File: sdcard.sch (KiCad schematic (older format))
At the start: 4 parts

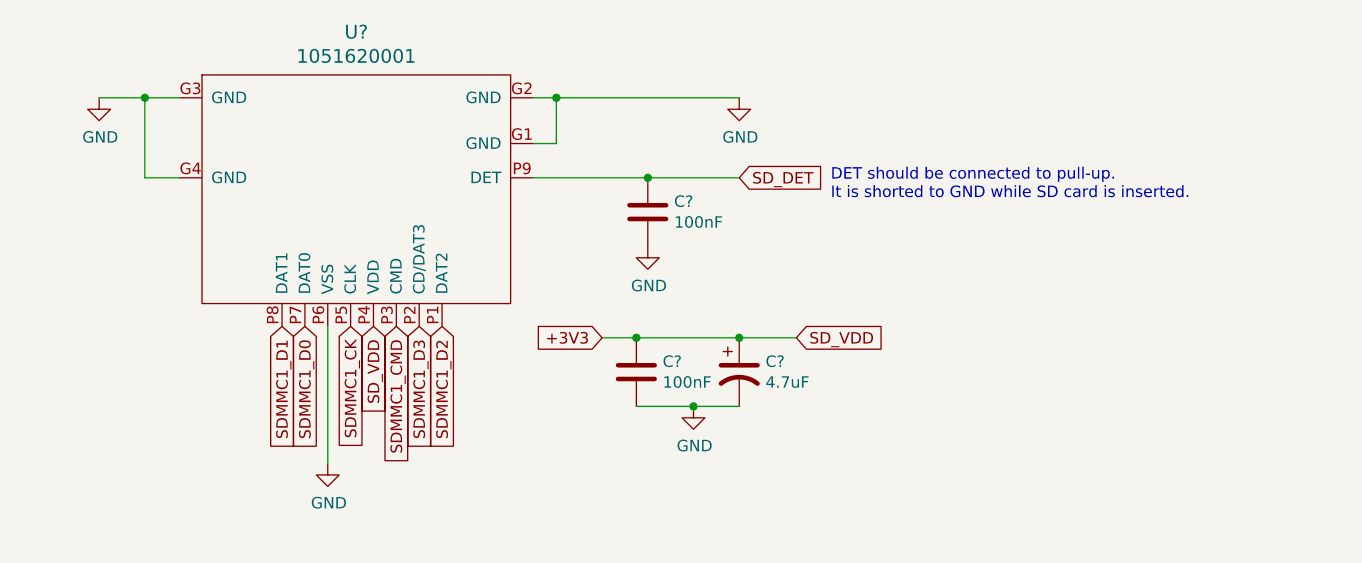
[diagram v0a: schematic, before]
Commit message: First proposed pin layout of SODIMM connector
Will need to add GPIO / ADC pins as needed, but let's wait to see if we don't
need to use more pins.

Double-checked and fixed CODEC and MCU's power supply.
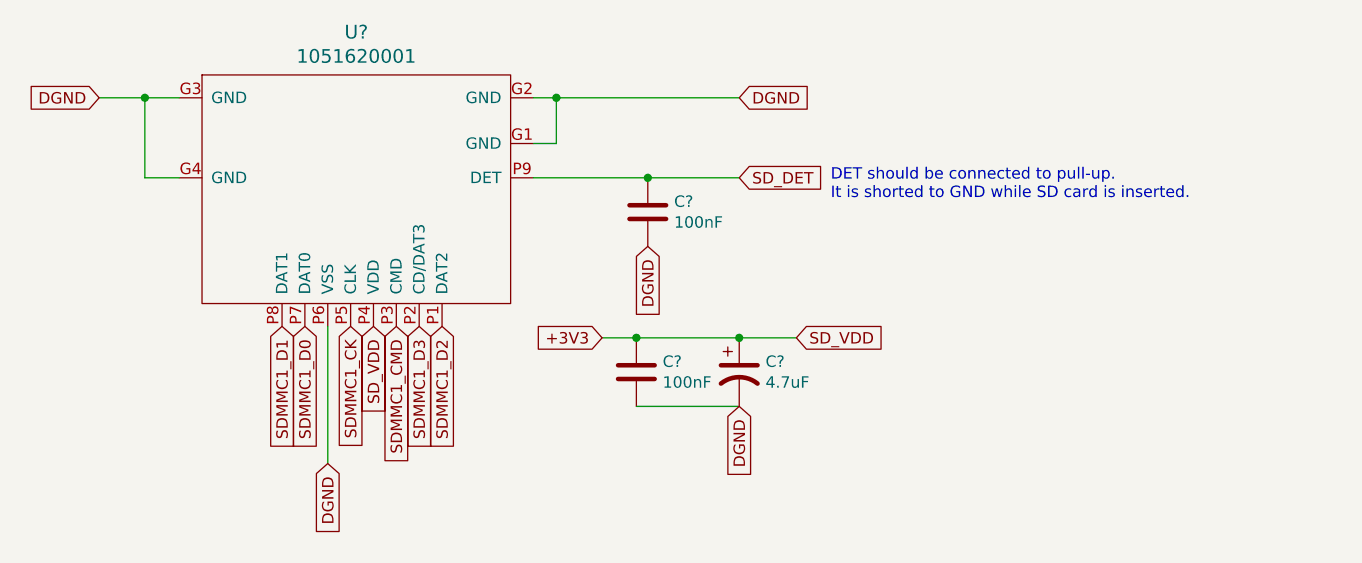
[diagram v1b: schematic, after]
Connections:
- net GND renamed DGND
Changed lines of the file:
@@
 $Descr A4 11693 8268
 encoding utf-8
-Sheet 8 12
+Sheet 8 13
 Title ""
 Date ""
@@
 	1    0    0    -1
 $EndComp
-$Comp
-L power:GND #PWR?
-U 1 1 5CFE73EC
-P 7200 3300
-F 0 "#PWR?" H 7200 3050 50  0001 C CNN
-F 1 "GND" H 7205 3127 50  0000 C CNN
-F 2 "" H 7200 3300 50  0001 C CNN
-F 3 "" H 7200 3300 50  0001 C CNN
-	1    7200 3300
-	1    0    0    -1
-$EndComp
 Wire Wire Line
 	6300 3300 6400 3300
@@
 Wire Wire Line
 	4600 3650 4750 3650
-$Comp
-L power:GND #PWR?
-U 1 1 5CFE745E
-P 4400 3300
-F 0 "#PWR?" H 4400 3050 50  0001 C CNN
-F 1 "GND" H 4405 3127 50  0000 C CNN
-F 2 "" H 4400 3300 50  0001 C CNN
-F 3 "" H 4400 3300 50  0001 C CNN
-	1    4400 3300
-	1    0    0    -1
-$EndComp
 Wire Wire Line
 	4400 3300 4600 3300
@@
 Text GLabel 5700 4300 3    50   Input ~ 0
 SDMMC1_CMD
-$Comp
-L power:GND #PWR?
-U 1 1 5CFE78C0
-P 5400 4900
-F 0 "#PWR?" H 5400 4650 50  0001 C CNN
-F 1 "GND" H 5405 4727 50  0000 C CNN
-F 2 "" H 5400 4900 50  0001 C CNN
-F 3 "" H 5400 4900 50  0001 C CNN
-	1    5400 4900
-	1    0    0    -1
-$EndComp
 Wire Wire Line
 	5400 4300 5400 4900
@@
 Wire Wire Line
 	6600 4350 6750 4350
-$Comp
-L power:GND #PWR?
-U 1 1 5CFEB0F7
-P 7000 4650
-F 0 "#PWR?" H 7000 4400 50  0001 C CNN
-F 1 "GND" H 7005 4477 50  0000 C CNN
-F 2 "" H 7000 4650 50  0001 C CNN
-F 3 "" H 7000 4650 50  0001 C CNN
-	1    7000 4650
-	1    0    0    -1
-$EndComp
 $Comp
 L Device:C C?
@@
 Wire Wire Line
 	7200 4350 7450 4350
-Wire Wire Line
-	7000 4650 7200 4650
-Connection ~ 7000 4650
-$Comp
-L power:GND #PWR?
-U 1 1 5CFEB709
-P 6800 3950
-F 0 "#PWR?" H 6800 3700 50  0001 C CNN
-F 1 "GND" H 6805 3777 50  0000 C CNN
-F 2 "" H 6800 3950 50  0001 C CNN
-F 3 "" H 6800 3950 50  0001 C CNN
-	1    6800 3950
-	1    0    0    -1
-$EndComp
 Connection ~ 6750 4350
 Wire Wire Line
 	6750 4350 7200 4350
-Wire Wire Line
-	6750 4650 7000 4650
 Wire Wire Line
 	6300 3650 6800 3650
@@
 Wire Wire Line
 	6800 3650 7200 3650
+Wire Wire Line
+	6750 4650 7200 4650
+Text GLabel 7200 4650 3    50   Input ~ 0
+DGND
+Text GLabel 7200 3300 2    50   Input ~ 0
+DGND
+Text GLabel 5400 4900 3    50   Input ~ 0
+DGND
+Text GLabel 4400 3300 0    50   Input ~ 0
+DGND
+Text GLabel 6800 3950 3    50   Input ~ 0
+DGND
 $EndSCHEMATC
